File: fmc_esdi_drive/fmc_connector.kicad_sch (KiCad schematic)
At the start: 1 part, among them J1 ASP-134604-01

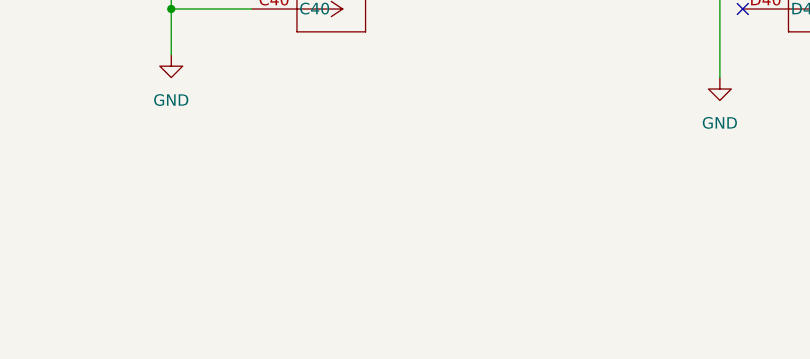
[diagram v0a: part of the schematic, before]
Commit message: PCB: Add hopeful board outline
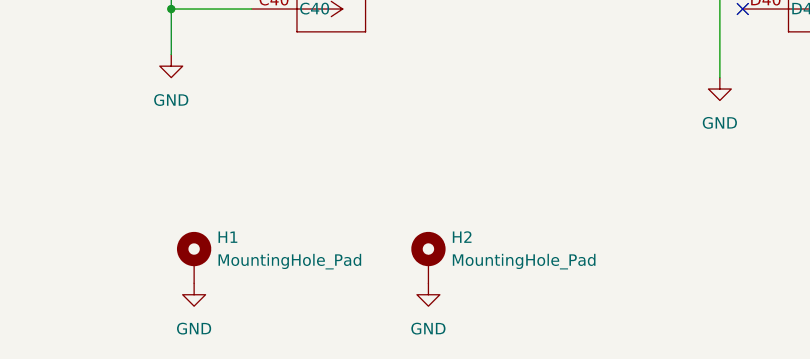
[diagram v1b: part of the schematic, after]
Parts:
- added H1, H2: MountingHole_Pad, MountingHole:MountingHole_2.7mm_M2.5_DIN965_Pad, symbol Mechanical:MountingHole_Pad
- J1: footprint CONN_ASP-134604-01_SAI -> custom:CONN_ASP-134604-01_SAI
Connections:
- net GND: now also H1.1, H2.1
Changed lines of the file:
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@@
       (effects (font (size 1.524 1.524)) (justify left))
     )
-    (property "Footprint" "CONN_ASP-134604-01_SAI" (at 111.76 40.64 0)
+    (property "Footprint" "custom:CONN_ASP-134604-01_SAI" (at 111.76 40.64 0)
       (effects (font (size 1.27 1.27) italic) hide)
     )
@@
     )
   )
+  (symbol (lib_id "Mechanical:MountingHole_Pad") (at 76.835 167.64 0) (unit 1)
+    (in_bom yes) (on_board yes) (dnp no) (fields_autoplaced)
+    (property "Reference" "H2" (at 79.375 165.1 0)
+      (effects (font (size 1.27 1.27)) (justify left))
+    )
+    (property "Value" "MountingHole_Pad" (at 79.375 167.64 0)
+      (effects (font (size 1.27 1.27)) (justify left))
+    )
+    (property "Footprint" "MountingHole:MountingHole_2.7mm_M2.5_DIN965_Pad" (at 76.835 167.64 0)
+      (effects (font (size 1.27 1.27)) hide)
+    )
+    (property "Datasheet" "~" (at 76.835 167.64 0)
+      (effects (font (size 1.27 1.27)) hide)
+    )
+    (pin "1")
+    (instances
+      (project "fmc_esdi_drive"
+        (path "/5573f2ee-e80c-4177-9891-e3b404cab47f/cf426c04-3745-4cda-8a66-0ee5961482e0"
+          (reference "H2") (unit 1)
+        )
+      )
+    )
+  )
   (symbol (lib_id "power:GND") (at 168.91 147.32 0) (unit 1)
     (in_bom yes) (on_board yes) (dnp no) (fields_autoplaced)
@@
         (path "/78e14509-c693-4ed5-9c5e-1c4dc2e11a3e"
           (reference "#PWR09") (unit 1)
+        )
+      )
+    )
+  )
+  (symbol (lib_id "Mechanical:MountingHole_Pad") (at 50.8 167.64 0) (unit 1)
+    (in_bom yes) (on_board yes) (dnp no) (fields_autoplaced)
+    (property "Reference" "H1" (at 53.34 165.1 0)
+      (effects (font (size 1.27 1.27)) (justify left))
+    )
+    (property "Value" "MountingHole_Pad" (at 53.34 167.64 0)
+      (effects (font (size 1.27 1.27)) (justify left))
+    )
+    (property "Footprint" "MountingHole:MountingHole_2.7mm_M2.5_DIN965_Pad" (at 50.8 167.64 0)
+      (effects (font (size 1.27 1.27)) hide)
+    )
+    (property "Datasheet" "~" (at 50.8 167.64 0)
+      (effects (font (size 1.27 1.27)) hide)
+    )
+    (pin "1")
+    (instances
+      (project "fmc_esdi_drive"
+        (path "/5573f2ee-e80c-4177-9891-e3b404cab47f/cf426c04-3745-4cda-8a66-0ee5961482e0"
+          (reference "H1") (unit 1)
         )
       )
@@
       (effects (font (size 1.524 1.524)) (justify left))
     )
-    (property "Footprint" "CONN_ASP-134604-01_SAI" (at 233.68 40.64 0)
+    (property "Footprint" "custom:CONN_ASP-134604-01_SAI" (at 233.68 40.64 0)
       (effects (font (size 1.27 1.27) italic) hide)
     )
@@
       (effects (font (size 1.524 1.524)) (justify left))
     )
-    (property "Footprint" "CONN_ASP-134604-01_SAI" (at 172.72 40.64 0)
+    (property "Footprint" "custom:CONN_ASP-134604-01_SAI" (at 172.72 40.64 0)
       (effects (font (size 1.27 1.27) italic) hide)
     )
@@
     )
   )
+  (symbol (lib_id "power:GND") (at 76.835 170.18 0) (unit 1)
+    (in_bom yes) (on_board yes) (dnp no) (fields_autoplaced)
+    (property "Reference" "#PWR06" (at 76.835 176.53 0)
+      (effects (font (size 1.27 1.27)) hide)
+    )
+    (property "Value" "GND" (at 76.835 175.26 0)
+      (effects (font (size 1.27 1.27)))
+    )
+    (property "Footprint" "" (at 76.835 170.18 0)
+      (effects (font (size 1.27 1.27)) hide)
+    )
+    (property "Datasheet" "" (at 76.835 170.18 0)
+      (effects (font (size 1.27 1.27)) hide)
+    )
+    (pin "1")
+    (instances
+      (project "fmc_esdi_drive"
+        (path "/5573f2ee-e80c-4177-9891-e3b404cab47f"
+          (reference "#PWR06") (unit 1)
+        )
+        (path "/5573f2ee-e80c-4177-9891-e3b404cab47f/cf426c04-3745-4cda-8a66-0ee5961482e0"
+          (reference "#PWR054") (unit 1)
+        )
+      )
+      (project "esdi_fmc"
+        (path "/78e14509-c693-4ed5-9c5e-1c4dc2e11a3e"
+          (reference "#PWR07") (unit 1)
+        )
+      )
+    )
+  )
+  (symbol (lib_id "power:GND") (at 50.8 170.18 0) (unit 1)
+    (in_bom yes) (on_board yes) (dnp no) (fields_autoplaced)
+    (property "Reference" "#PWR06" (at 50.8 176.53 0)
+      (effects (font (size 1.27 1.27)) hide)
+    )
+    (property "Value" "GND" (at 50.8 175.26 0)
+      (effects (font (size 1.27 1.27)))
+    )
+    (property "Footprint" "" (at 50.8 170.18 0)
+      (effects (font (size 1.27 1.27)) hide)
+    )
+    (property "Datasheet" "" (at 50.8 170.18 0)
+      (effects (font (size 1.27 1.27)) hide)
+    )
+    (pin "1")
+    (instances
+      (project "fmc_esdi_drive"
+        (path "/5573f2ee-e80c-4177-9891-e3b404cab47f"
+          (reference "#PWR06") (unit 1)
+        )
+        (path "/5573f2ee-e80c-4177-9891-e3b404cab47f/cf426c04-3745-4cda-8a66-0ee5961482e0"
+          (reference "#PWR053") (unit 1)
+        )
+      )
+      (project "esdi_fmc"
+        (path "/78e14509-c693-4ed5-9c5e-1c4dc2e11a3e"
+          (reference "#PWR07") (unit 1)
+        )
+      )
+    )
+  )
   (symbol (lib_id "custom:ASP-134604-01") (at 57.15 40.64 0) (unit 1)
     (in_bom yes) (on_board yes) (dnp no)
@@
       (effects (font (size 1.524 1.524)) (justify left))
     )
-    (property "Footprint" "CONN_ASP-134604-01_SAI" (at 57.15 40.64 0)
+    (property "Footprint" "custom:CONN_ASP-134604-01_SAI" (at 57.15 40.64 0)
       (effects (font (size 1.27 1.27) italic) hide)
     )

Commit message: Finish FMC adapter PCB
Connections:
- net CMD_COMPLETE_B_FMC: now also J1.H32; no longer J1.G31
- net DRIVE_SELECTED_B_FMC: now also J1.H31; no longer J1.G30
- net INDEX_UNGATED_B_FMC: now also J1.G30; no longer J1.H32
- net READ_CLOCK_A_FMC: now also J1.H34; no longer J1.G33
- net READ_CLOCK_B_FMC: now also J1.H37; no longer J1.G36
- net READ_DATA_A_FMC: now also J1.G33; no longer J1.H34
- net READ_DATA_B_FMC: now also J1.G36; no longer J1.H37
- net SECTOR_UNGATED_B_FMC: now also J1.G31; no longer J1.H31
- net WRITE_CLOCK_A_FMC: now also J1.G18; no longer J1.H16
- net WRITE_CLOCK_B_FMC: now also J1.G21; no longer J1.H19
- net WRITE_DATA_A_FMC: now also J1.H16; no longer J1.G18
- net WRITE_DATA_B_FMC: now also J1.H19; no longer J1.G21
